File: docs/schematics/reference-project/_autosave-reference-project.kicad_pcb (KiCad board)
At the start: 2 copper layers, 22 parts, among them J1 UART, Q1 MMBT3904, SW1 INPUT_0, SW2 INPUT_1, SW3 INPUT_2, SW4 INPUT_3, SW5 INPUT_4, SW6 INPUT_5, SW7 RESET, U1 74HC165D, U2 ATTINY85-20PU

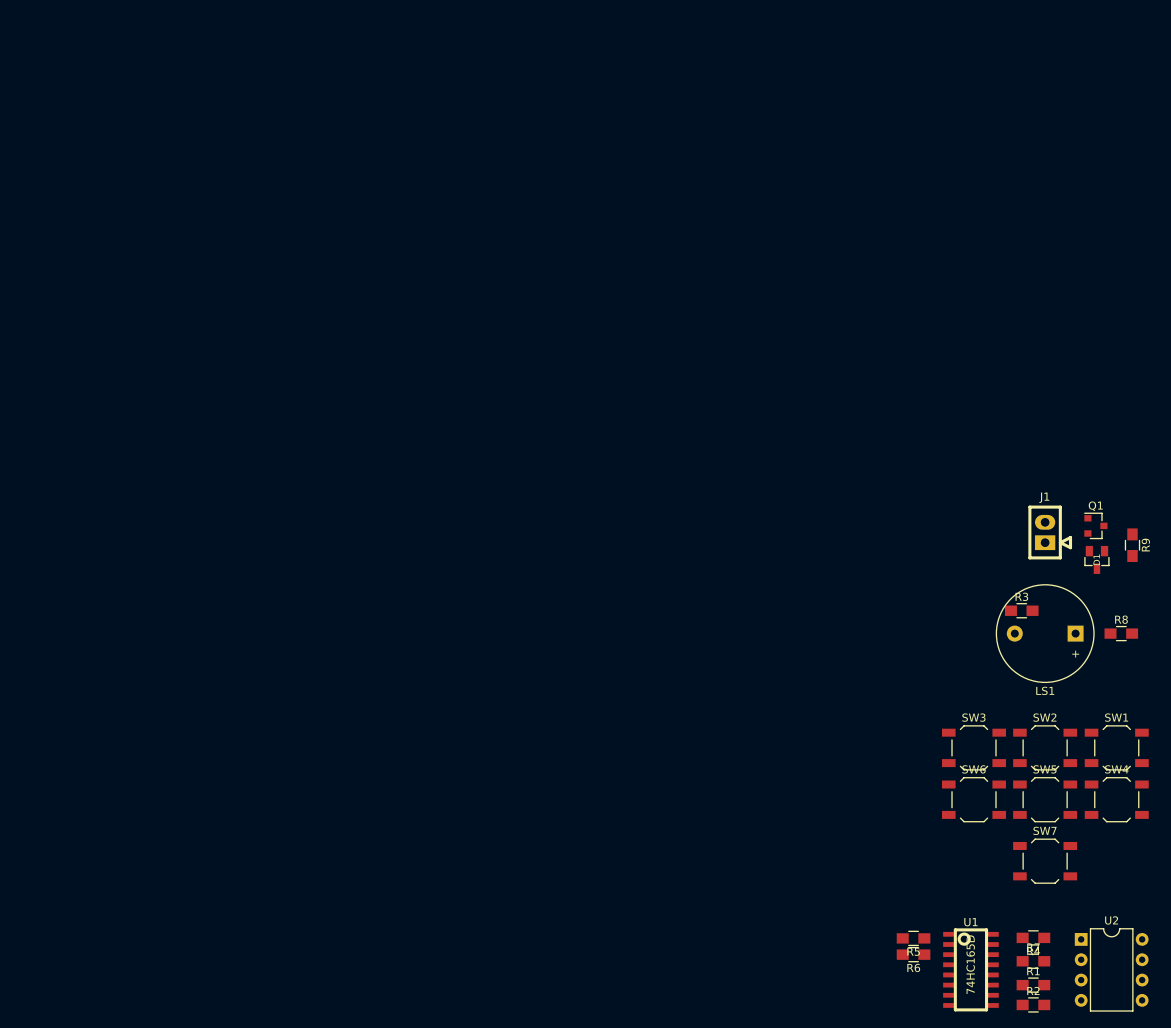
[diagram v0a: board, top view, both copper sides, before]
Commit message: New version of schematics.
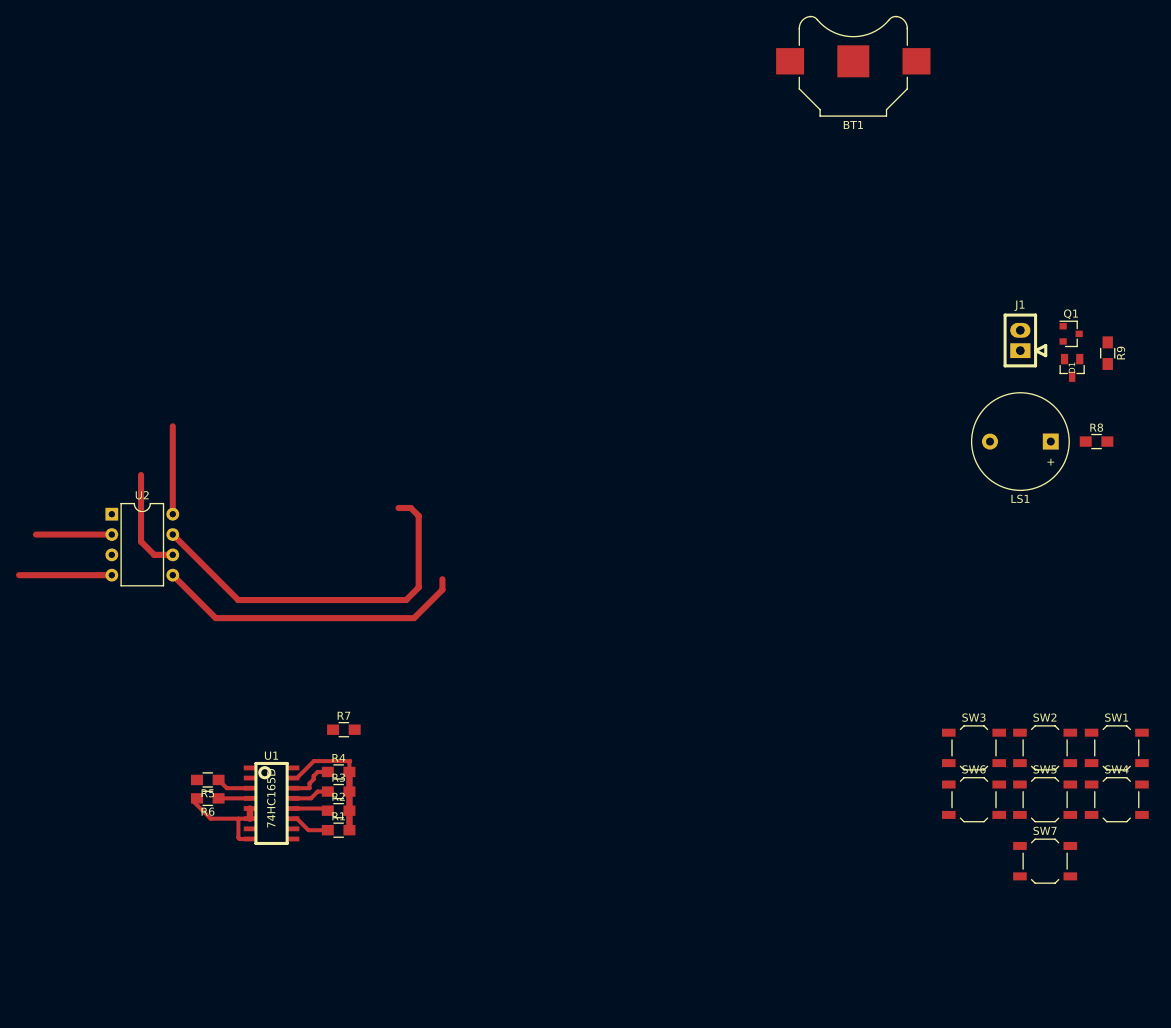
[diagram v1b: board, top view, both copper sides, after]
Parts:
- added BT1: CELL, Battery_Holders:Keystone_3000_1x12mm-CoinCell, F.Cu at (135.0, 20.0)
- moved U2 132.3 mm to (42.3, 76.6)
- moved R7 90.9 mm to (71.3, 103.5)
- moved R5 90.4 mm to (54.3, 109.8)
- moved R6 90.4 mm to (54.3, 112.1)
- moved R2 90.2 mm to (70.7, 113.6)
- moved U1 89.9 mm to (62.3, 112.1)
- moved R4 89.3 mm to (70.7, 108.8), turned to 0 degrees
- moved R1 89.0 mm to (70.7, 116.1)
- moved R3 88.3 mm to (70.7, 111.3)
- moved D1 24.2 mm to (162.4, 58.3)
- moved J1 24.2 mm to (155.9, 54.9)
- moved Q1 24.2 mm to (162.3, 54.0)
- moved LS1 24.2 mm to (159.7, 67.5)
- moved R8 24.2 mm to (165.4, 67.5)
- moved R9 24.2 mm to (166.8, 56.5)
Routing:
- net Net-(U1-Pad1): track 0.00 -> 46.7 mm
- net GND: track 0.00 -> 41.4 mm
- net Net-(U1-Pad9): track 0.00 -> 38.7 mm
- net Net-(D1-Pad1): track 0.00 -> 13.0 mm
- net +3V3: track 0.00 -> 11.5 mm
- net Net-(R7-Pad2): track 0.00 -> 9.48 mm
- net Net-(R4-Pad1): track 0.00 -> 5.76 mm
- net Net-(R1-Pad1): track 0.00 -> 4.93 mm
- net Net-(R3-Pad1): track 0.00 -> 4.68 mm
- net Net-(R2-Pad1): track 0.00 -> 4.44 mm
- net Net-(R5-Pad1): track 0.00 -> 4.35 mm
- net Net-(R6-Pad1): track 0.00 -> 3.92 mm
